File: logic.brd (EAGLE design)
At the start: 37.4 x 32.5 mm, 10 parts, among them CON1 PINHEAD_1X10-2, CON2 PINHEAD_1X10-2, CON3 PINHEAD_1X02-2, CON4 PINHEAD_1X02-2, CON5 PINHEAD_1X02-2, CON7 PINHEAD_1X07-2

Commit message: UAVCAN logo
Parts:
- added U$3: (no value), logo:UAVCAN_9X2.5
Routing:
- net GPIO1: track 37.3 -> 33.9 mm
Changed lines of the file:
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@@
 <?xml version="1.0" encoding="utf-8"?>
 <!DOCTYPE eagle SYSTEM "eagle.dtd">
-<eagle version="9.2.2">
+<eagle version="9.3.2">
 <drawing>
 <settings>
@@
 <setting verticaltext="up"/>
 </settings>
-<grid distance="0.1" unitdist="mm" unit="mm" style="lines" multiple="1" display="no" altdistance="5" altunitdist="mil" altunit="mil"/>
+<grid distance="0.1" unitdist="mm" unit="mm" style="lines" multiple="1" display="yes" altdistance="5" altunitdist="mil" altunit="mil"/>
 <layers>
 <layer number="1" name="Top" color="4" fill="1" visible="yes" active="yes"/>
@@
 </layers>
 <board>
-<fusionsync huburn="a.cGVyc29uYWw6dWUyYWE4ZDY4" projecturn="a.cGVyc29uYWw6dWUyYWE4ZDY4IzIwMTgxMTAxMTU3ODMxMTgx" f3durn="urn:adsk.wipprod:dm.lineage:0Eun1Ys4QIydmOHYlR5lhA" pcbguid="f6d64cec-dc36-4f55-bc1b-b0017d6e68a5" lastpulledtime="" lastsyncedchangeguid="f59d5b97-4dd3-de67-a9ba-2ef64862d5c8"/>
+<fusionsync huburn="a.cGVyc29uYWw6dWUyYWE4ZDY4" projecturn="a.cGVyc29uYWw6dWUyYWE4ZDY4IzIwMTgxMTAxMTU3ODMxMTgx" f3durn="urn:adsk.wipprod:dm.lineage:0Eun1Ys4QIydmOHYlR5lhA" pcbguid="f6d64cec-dc36-4f55-bc1b-b0017d6e68a5" lastpulledtime="" lastsyncedchangeguid="bff609ef-31de-0e35-d9a9-38f5aedecdc5"/>
 <plain>
 <wire x1="0" y1="0" x2="0" y2="21" width="0.1524" layer="49" style="shortdash"/>
@@
 </element>
 <element name="U$4" library="logo" library_urn="urn:adsk.eagle:library:6668987" package="DRAGON-18X7" value="" x="3.6" y="3.2" smashed="yes" rot="MR315"/>
+<element name="U$3" library="logo" library_urn="urn:adsk.eagle:library:6668987" package="UAVCAN_9X2.5" value="" x="4.7" y="-16.1" smashed="yes" rot="MR0"/>
 </elements>
 <signals>
@@
 <signal name="GPIO1">
 <contactref element="MODULE1" pad="27"/>
-<wire x1="-10.1161" y1="-10.6161" x2="-9" y2="-9.5" width="0.2" layer="16"/>
-<wire x1="-12.0087" y1="-10.6161" x2="-10.1161" y2="-10.6161" width="0.2" layer="16"/>
 <contactref element="CON7" pad="3"/>
 <wire x1="-2" y1="-12.2" x2="-4" y2="-10.2" width="0.15" layer="1"/>

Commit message: let there be a giant hole in the middle of the PCB
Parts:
- removed U$2: (no value), logo:OSHW-10.5X11.5
- removed U$4: (no value), logo:DRAGON-18X7
- added U$5: (no value), logo:DRAGON-15X6
- moved U$1 12.8 mm to (-6.19, 9.24), turned to 315 degrees
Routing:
- net PHASE_B_GND: track 22.4 -> 24.4 mm
- net PHASE_C_GATE_HIGH: track 28.5 -> 30.1 mm
- net PHASE_B_GATE_LOW: track 26.1 -> 27.5 mm
- net PHASE_B: track 29.6 -> 30.9 mm, vias 0 -> 1
- net PHASE_B_GATE_HIGH: track 33.5 -> 34.7 mm, vias 0 -> 1
- net VDD_5V: track 67.0 -> 68.0 mm
- net PHASE_C: track 33.5 -> 32.8 mm
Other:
- outline, holes or cut-outs redrawn
- board text added: "SadullliL2"
- board text removed: "SadullliL"

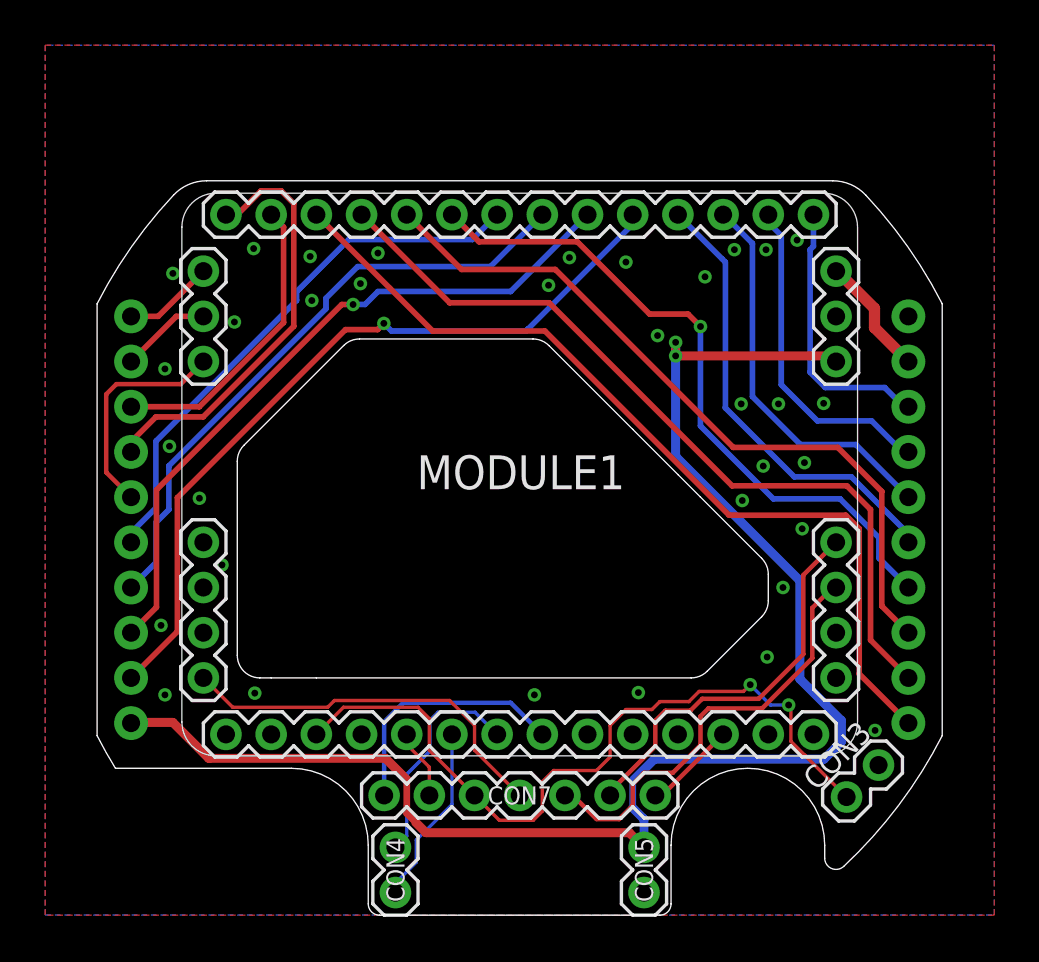
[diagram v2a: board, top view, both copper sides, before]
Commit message: migration to the latest version of mitochondrik library
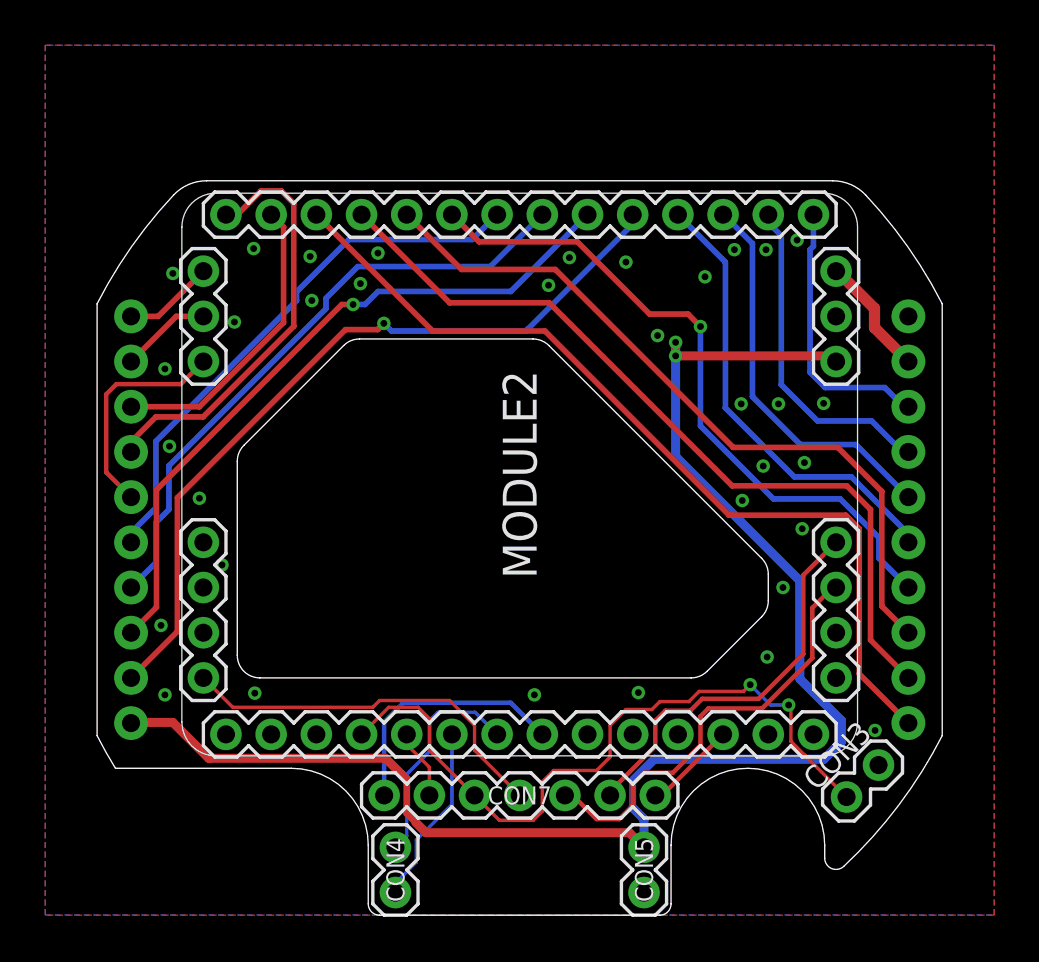
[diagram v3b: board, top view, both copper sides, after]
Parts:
- MODULE2: value MITOHONDRIQUE-TH -> MITOHONDRIQUE_V0.2-TH
- renumbered MODULE1 to MODULE2
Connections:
- removed net GPIO2: MODULE2.28
- net ADJ: now also MODULE2.26; no longer MODULE2.29
- net BEC_ENABLE: now also MODULE2.21; no longer MODULE2.24
- net BLUE: now also MODULE2.29; no longer MODULE2.32
- net CAN1_LED: now also MODULE2.33; no longer MODULE2.36
- net CAN1_RX: now also MODULE2.38; no longer MODULE2.41
- net CAN1_TX: now also MODULE2.39; no longer MODULE2.42
- net GND: now also MODULE2.41; no longer MODULE2.2
- net GPIO1: now also MODULE2.25; no longer MODULE2.27
- net GREEN: now also MODULE2.28; no longer MODULE2.31
- net PHASE_A: now also MODULE2.2; no longer MODULE2.5
- net PHASE_A_CURRENT_SHUNT_N: now also MODULE2.13; no longer MODULE2.16
- net PHASE_A_CURRENT_SHUNT_P: now also MODULE2.14; no longer MODULE2.17
- net PHASE_A_GATE_HIGH: now also MODULE2.1; no longer MODULE2.4
- net PHASE_A_GATE_LOW: now also MODULE2.3; no longer MODULE2.6
- net PHASE_A_GND: now also MODULE2.4; no longer MODULE2.7
- net PHASE_B: now also MODULE2.6; no longer MODULE2.9
- net PHASE_B_CURRENT_SHUNT_N: now also MODULE2.15; no longer MODULE2.18
- net PHASE_B_CURRENT_SHUNT_P: now also MODULE2.16; no longer MODULE2.19
- net PHASE_B_GATE_HIGH: now also MODULE2.5; no longer MODULE2.8
- net PHASE_B_GATE_LOW: now also MODULE2.7; no longer MODULE2.10
- net PHASE_B_GND: now also MODULE2.8; no longer MODULE2.11
- net PHASE_C: now also MODULE2.10; no longer MODULE2.13
- net PHASE_C_GATE_HIGH: now also MODULE2.9; no longer MODULE2.12
- net PHASE_C_GATE_LOW: now also MODULE2.11; no longer MODULE2.14
- net PHASE_C_GND: now also MODULE2.12; no longer MODULE2.15
- net RED: now also MODULE2.27; no longer MODULE2.30
- net TEMPERATURE_SENSOR: now also MODULE2.17; no longer MODULE2.20
- net VDC: now also MODULE2.42; no longer MODULE2.3
- net VDD_5V: now also MODULE2.40; no longer MODULE2.1
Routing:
- net GPIO1: track 33.9 -> 31.9 mm
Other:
- outline, holes or cut-outs redrawn
